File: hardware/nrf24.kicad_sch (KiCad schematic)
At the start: 20 parts, among them U2 nRF24L01P, Y1 16MHz

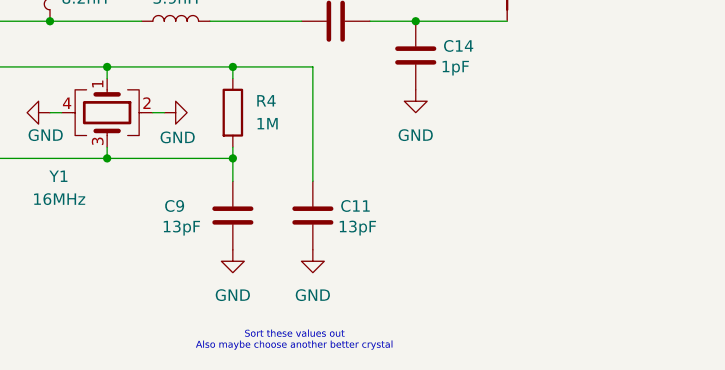
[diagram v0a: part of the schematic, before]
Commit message: Routed crystal circuitry
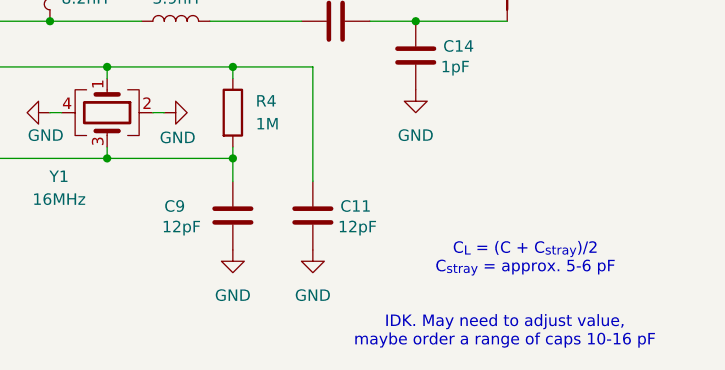
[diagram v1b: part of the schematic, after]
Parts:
- C11, C9: value 13pF -> 12pF
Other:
- note added: "C_{L} = (C + C_{stray})/2 C_{stray} = approx. 5-6 pF"
- note added: "IDK. May need to adjust value, maybe order a range of caps 10-16 pF"
- note removed: "Sort these values out Also maybe choose another better crystal"
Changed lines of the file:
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@@
+		)
+	)
+	(text "C_{L} = (C + C_{stray})/2\nC_{stray} = approx. 5-6 pF"
+		(exclude_from_sim no)
+		(at 209.042 126.746 0)
+		(effects
+			(font
+				(size 1.27 1.27)
+			)
 		)
 	)
@@
 		)
 	)
-	(text "Sort these values out\nAlso maybe choose another better crystal"
-		(exclude_from_sim no)
-		(at 183.388 135.89 0)
+	(text "IDK. May need to adjust value,\nmaybe order a range of caps 10-16 pF"
+		(exclude_from_sim no)
+		(at 206.756 134.874 0)
 		(effects
 			(font
-				(size 0.762 0.762)
+				(size 1.27 1.27)
 			)
 		)
@@
 			)
 		)
-		(property "Value" "13pF"
+		(property "Value" "12pF"
 			(at 188.214 123.19 0)
 			(effects
@@
 			)
 		)
-		(property "Datasheet" "https://img.pcbx.com/dev/file/part/spec/X322512MSB4SI-Yangxing%20Technology.pdf"
+		(property "Datasheet" "https://jlcpcb.com/api/file/downloadByFileSystemAccessId/8588879072148017152"
 			(at 162.56 110.49 0)
 			(effects
@@
 			)
 		)
-		(property "Value" "13pF"
+		(property "Value" "12pF"
 			(at 168.656 123.19 0)
 			(effects

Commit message: Added part numbers for ~1/2 of components
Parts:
- C4, C5: LCSC Part # (none) -> C59461; MPN (none) -> CL10A226MQ8NRNC
- C6: LCSC Part # (none) -> C59461
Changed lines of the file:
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@@
 			)
 		)
-		(property "Datasheet" "~"
+		(property "Datasheet" "https://www.lcsc.com/datasheet/lcsc_datasheet_2304140030_Samsung-Electro-Mechanics-CL10A226MQ8NRNC_C59461.pdf"
 			(at 72.39 73.66 0)
 			(effects
@@
 			)
 		)
-		(property "Description" "Unpolarized capacitor"
+		(property "Description" "6.3V 22uF X5R ±20% 0603 Multilayer Ceramic Capacitors MLCC - SMD/SMT ROHS"
+			(at 72.39 73.66 0)
+			(effects
+				(font
+					(size 1.27 1.27)
+				)
+				(hide yes)
+			)
+		)
+		(property "MPN" "CL10A226MQ8NRNC"
+			(at 72.39 73.66 0)
+			(effects
+				(font
+					(size 1.27 1.27)
+				)
+				(hide yes)
+			)
+		)
+		(property "LCSC Part #" "C59461"
 			(at 72.39 73.66 0)
 			(effects
@@
 			)
 		)
-		(property "Datasheet" "~"
+		(property "Datasheet" "https://www.lcsc.com/datasheet/lcsc_datasheet_2304140030_Samsung-Electro-Mechanics-CL10A226MQ8NRNC_C59461.pdf"
 			(at 86.36 73.66 0)
 			(effects
@@
 			)
 		)
-		(property "Description" "Unpolarized capacitor"
+		(property "Description" "6.3V 22uF X5R ±20% 0603 Multilayer Ceramic Capacitors MLCC - SMD/SMT ROHS"
+			(at 86.36 73.66 0)
+			(effects
+				(font
+					(size 1.27 1.27)
+				)
+				(hide yes)
+			)
+		)
+		(property "LCSC Part #" "C59461"
 			(at 86.36 73.66 0)
 			(effects
@@
 			)
 		)
-		(property "Datasheet" "~"
+		(property "Datasheet" "https://www.lcsc.com/datasheet/lcsc_datasheet_2304140030_Samsung-Electro-Mechanics-CL10A226MQ8NRNC_C59461.pdf"
 			(at 60.96 73.66 0)
 			(effects
@@
 			)
 		)
-		(property "Description" "Unpolarized capacitor"
+		(property "Description" "6.3V 22uF X5R ±20% 0603 Multilayer Ceramic Capacitors MLCC - SMD/SMT ROHS"
 			(at 60.96 73.66 0)
 			(effects
+				(font
+					(size 1.27 1.27)
+				)
+				(hide yes)
+			)
+		)
+		(property "LCSC Part #" "C59461"
+			(at 60.96 73.66 0)
+			(effects
+				(font
+					(size 1.27 1.27)
+				)
+				(hide yes)
+			)
+		)
+		(property "MPN" "CL10A226MQ8NRNC"
+			(at 60.96 73.66 0)
+			(effects

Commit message: Added MPN's for rest of components
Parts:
- C10: LCSC Part # (none) -> C1604; MPN (none) -> 0603B222K500NT
- C11, C9: LCSC Part # (none) -> C519482; MPN (none) -> CC0603FRNPO9BN120
- C12: LCSC Part # (none) -> C1669; MPN (none) -> 0603CG4R7C500NT
- C13: MPN (none) -> HH18N1R5B500CT
- C14: MPN (none) -> HH18N1R0B500CT
- C27: LCSC Part # (none) -> C1588; MPN (none) -> CL10B102KB8NNNC
- C7: LCSC Part # (none) -> C21117; MPN (none) -> CL10B333KB8NNNC
- C8: LCSC Part # (none) -> C57112; MPN (none) -> 0603B103K500NT
- L1: MPN (none) -> BSCQ000603032N7B00
- L2: MPN (none) -> BSCQ000603038N2H00
- L3: MPN (none) -> BSCQ000603033N9B00
- R3: LCSC Part # (none) -> C31850; MPN (none) -> 0603WAF2202T5E
- R4: LCSC Part # (none) -> C22935; MPN (none) -> 0603WAF1004T5E
- U2: LCSC Part # (none) -> C8791; MPN (none) -> NRF24L01P-R
- Y1: LCSC Part # (none) -> C13738; MPN (none) -> X322516MLB4SI

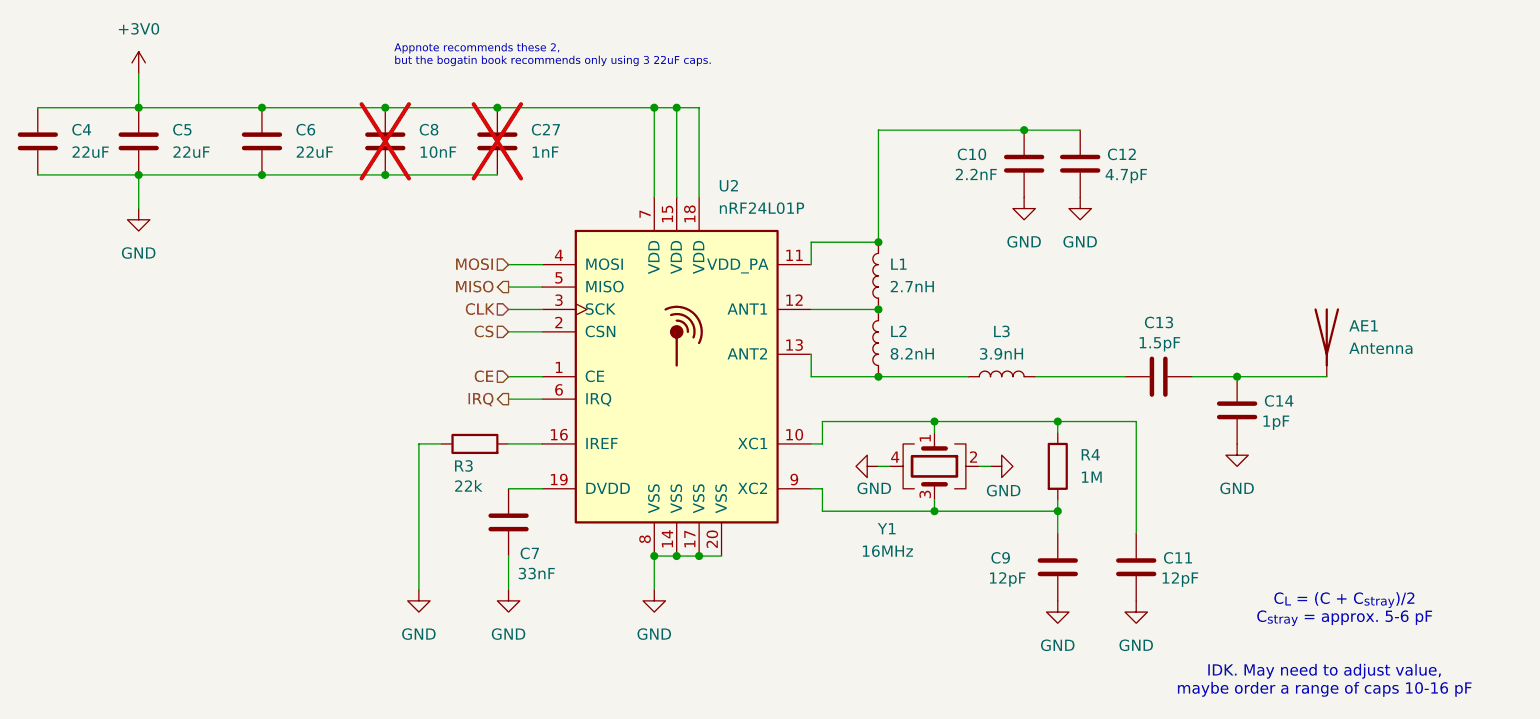
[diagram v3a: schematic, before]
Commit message: Added thermal pad connection to schematic
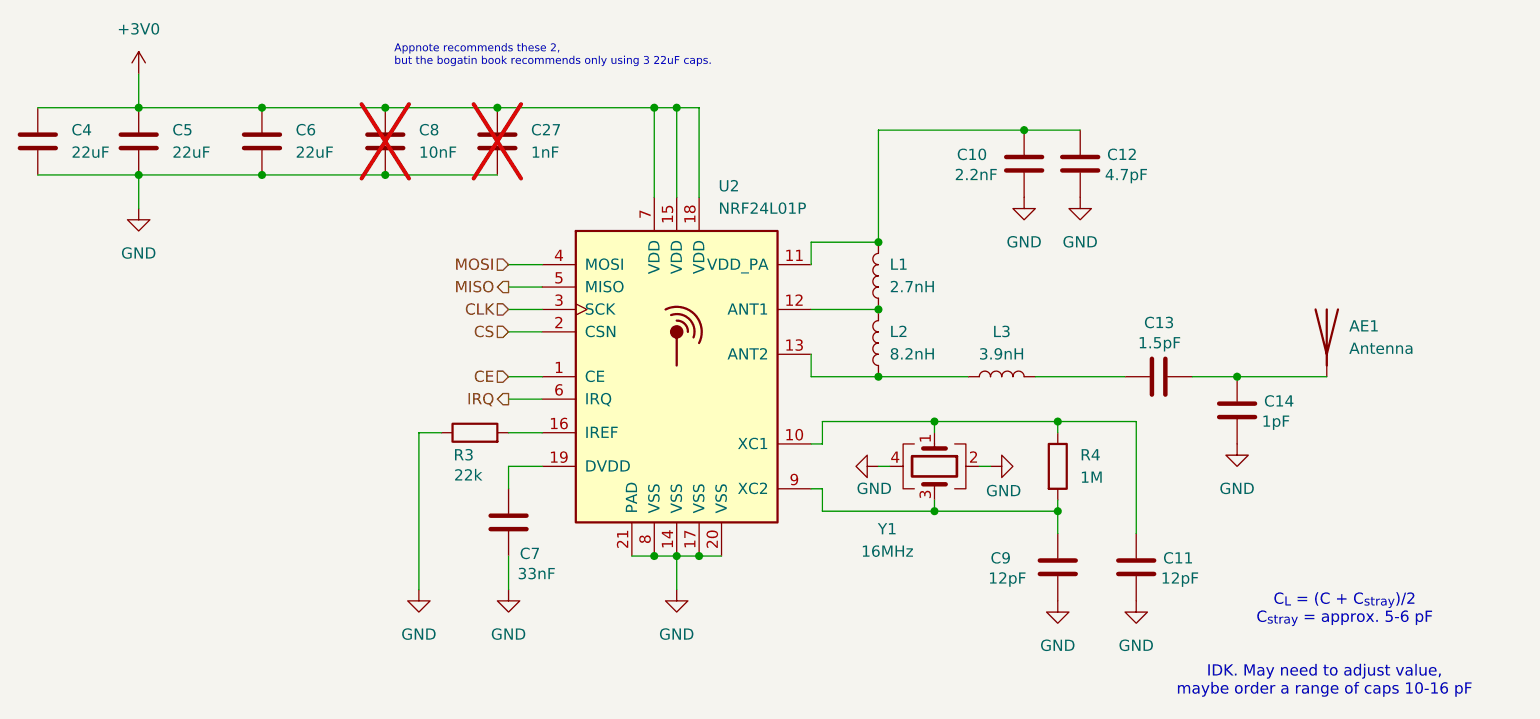
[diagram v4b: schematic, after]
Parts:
- removed U2: nRF24L01P, heli-footprints:NRF24L01_HandSolder_SpecialPad, symbol RF:nRF24L01P
- added U2: NRF24L01P, heli-footprints:NRF24L01_HandSolder_SpecialPad, symbol heli_symbols:NRF24L01P
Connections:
- net +3V0: now also U2.15 (VDD), U2.18 (VDD), U2.7 (VDD)
- net CE: now also U2.1 (CE)
- net CLK: now also U2.3 (SCK)
- net CS: now also U2.2 (CSN)
- net GND: now also U2.14 (VSS), U2.17 (VSS), U2.20 (VSS), U2.21 (PAD), U2.8 (VSS)
- net IRQ: now also U2.6 (IRQ)
- net MISO: now also U2.5 (MISO)
- net MOSI: now also U2.4 (MOSI)
- net at C11.1, R4.1, Y1.1: now also U2.10 (XC1)
- net at C10.1, C12.1, L1.2: now also U2.11 (VDD_PA)
- net at L1.1, L2.2: now also U2.12 (ANT1)
- net at L2.1, L3.1: now also U2.13 (ANT2)
- net at R3.2: now also U2.16 (IREF)
- net at C7.1: now also U2.19 (DVDD)
- net at C9.1, R4.2, Y1.3: now also U2.9 (XC2)
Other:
- moved on the sheet: R3

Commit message: Updates to fields for PCBWay BOM generation
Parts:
- AE1: now left out of the parts list
- C6: MPN (none) -> CL10A226MQ8NRNC
- U2: LCSC Part # (none) -> C8791; MPN (none) -> NRF24L01P-R
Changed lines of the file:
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@@
 		(unit 1)
 		(exclude_from_sim no)
-		(in_bom yes)
+		(in_bom no)
 		(on_board yes)
 		(dnp no)
@@
 			)
 		)
+		(property "MPN" "CL10A226MQ8NRNC"
+			(at 86.36 73.66 0)
+			(effects
+				(font
+					(size 1.27 1.27)
+				)
+				(hide yes)
+			)
+		)
 		(pin "2"
 		)
@@
 			(at 133.35 100.33 0)
 			(effects
+				(font
+					(size 1.27 1.27)
+				)
+				(hide yes)
+			)
+		)
+		(property "LCSC Part #" "C8791"
+			(at 133.35 100.33 0)
+			(effects
+				(font
+					(size 1.27 1.27)
+				)
+				(hide yes)
+			)
+		)
+		(property "MPN" "NRF24L01P-R"
+			(at 133.35 100.33 0)
+			(effects
